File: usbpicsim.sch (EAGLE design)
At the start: 11 parts, among them U1 PIC16F1455-I/ST

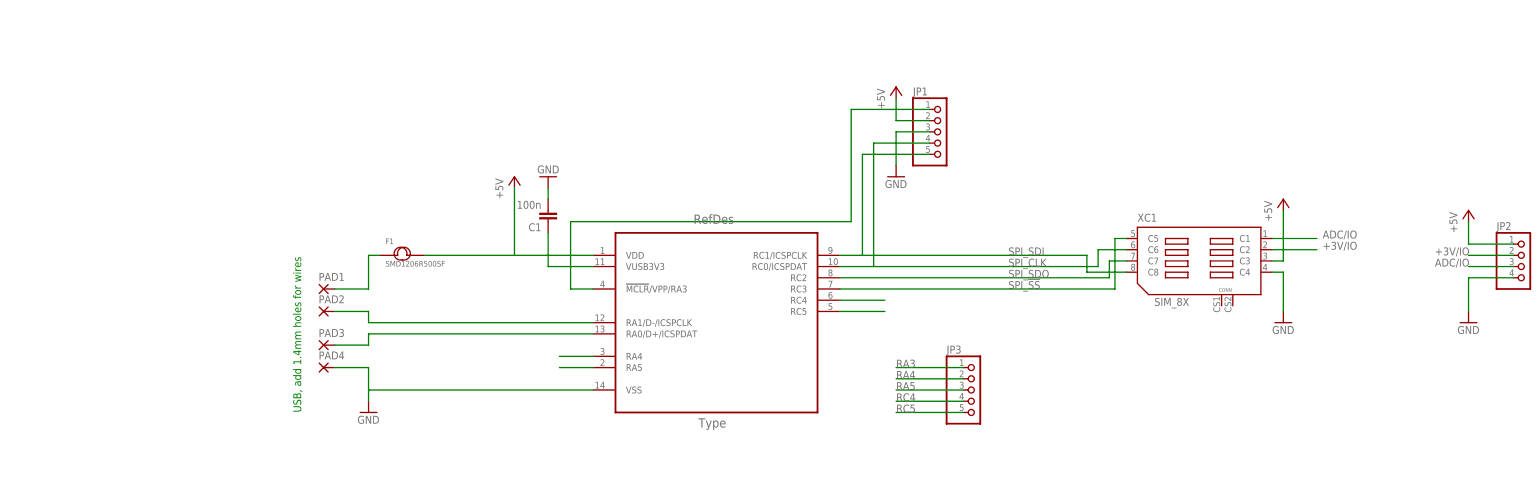
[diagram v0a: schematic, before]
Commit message: Use PIC LF (low voltage), add LDO
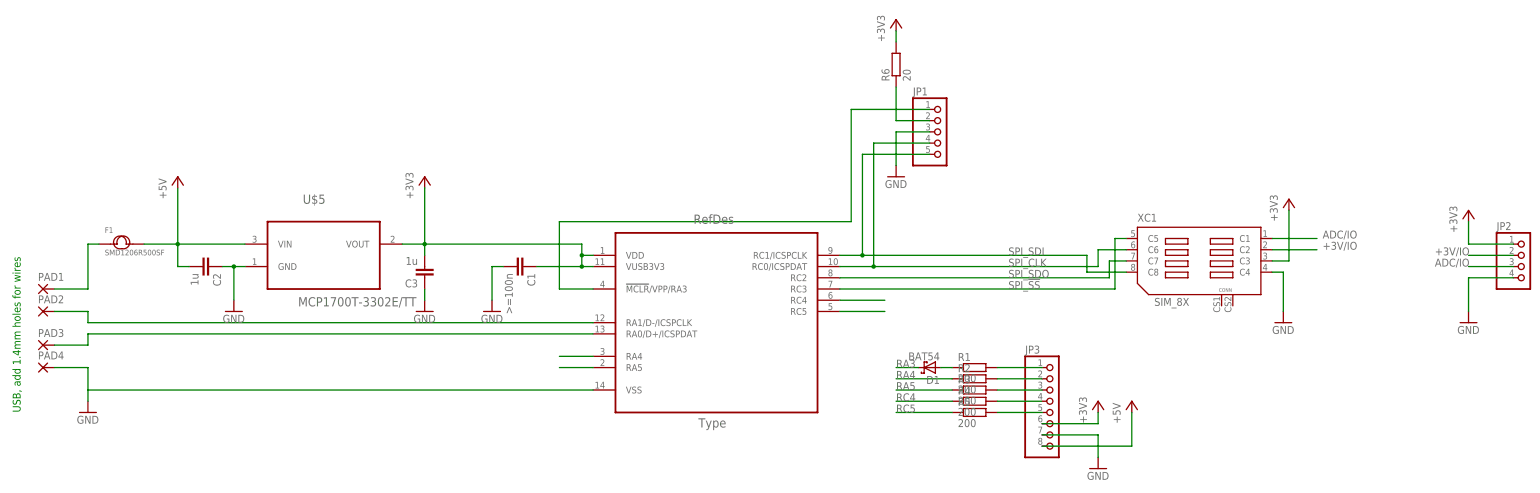
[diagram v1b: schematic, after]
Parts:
- added C2, C3: 1u, rcl:C-EUC0603
- added D1: BAT54, diode:BAT54
- added R1, R2, R3, R4, R5: 200, tagps:R-EU_R0603
- added R6: 20, tagps:R-EU_R0603
- added U$5: MCP1700T-3302E/TT, usbpiclib:MCP1700T-3302E/TT
- C1: value 100n -> >=100n
- JP3: device pinhead:PINHD-1X5 -> pinhead:PINHD-1X8
- U1: value PIC16F1455-I/ST -> PIC16LF1455-I/ST; device usbpiclib:PIC16F1455-I/ST -> usbpiclib:PIC16LF1455-I/ST
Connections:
- new net +3V3: C1.1, C3.2, JP2.1, JP3.6, R6.2, U$5.VOUT, U1.VDD, U1.VUSB3V3, XC1.C3
- new net N$10: D1.A, R1.1
- new net N$4: JP3.5, R5.2
- new net N$6: JP3.1, R1.2
- new net N$7: JP3.2, R2.2
- new net N$8: JP3.4, R4.2
- new net N$9: JP1.2, R6.1
- net +3V/IO: now also JP2.2
- net +5V: now also C2.2, JP3.8, U$5.VIN; no longer JP1.2, JP2.1, U1.VDD, XC1.C3
- net ADC/IO: now also JP2.3
- net GND: now also C2.1, C3.1, JP3.7, U$5.GND
- net N$1: now also JP3.3, R3.2; no longer C1.1, U1.VUSB3V3
- net RA3: now also D1.C; no longer JP3.1
- net RA4: now also R2.1; no longer JP3.2
- net RA5: now also R3.1; no longer JP3.3
- net RC4: now also R4.1; no longer JP3.4
- net RC5: now also R5.1; no longer JP3.5
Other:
- moved on the sheet: C1, F1, PAD1, PAD2, PAD3, PAD4

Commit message: Polish scheme, board
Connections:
- net N$10 renamed RA3@1
- net N$6 renamed RA3@2
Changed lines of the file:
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@@
 <setting verticaltext="up"/>
 </settings>
-<grid distance="0.1" unitdist="inch" unit="inch" style="lines" multiple="1" display="yes" altdistance="0.01" altunitdist="inch" altunit="inch"/>
+<grid distance="0.1" unitdist="inch" unit="inch" style="lines" multiple="1" display="no" altdistance="0.01" altunitdist="inch" altunit="inch"/>
 <layers>
 <layer number="1" name="Top" color="4" fill="1" visible="no" active="no"/>
@@
 </segment>
 </net>
-<net name="N$6" class="0">
+<net name="RA3@2" class="0">
 <segment>
 <pinref part="JP3" gate="A" pin="1"/>
@@
 </segment>
 </net>
-<net name="N$10" class="0">
+<net name="RA3@1" class="0">
 <segment>
 <pinref part="R1" gate="G$1" pin="1"/>

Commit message: Final usbpicsim board tuning
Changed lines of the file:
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@@
 <wire x1="-119.38" y1="40.64" x2="-111.76" y2="40.64" width="0.1524" layer="91"/>
 <wire x1="-111.76" y1="40.64" x2="-111.76" y2="35.56" width="0.1524" layer="91"/>
+<junction x="-111.76" y="35.56"/>
 </segment>
 <segment>

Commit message: Add TODO comment
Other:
- note added: "Pridat diodu jako ochranu proti prepolovani"
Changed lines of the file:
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@@
 <plain>
 <text x="-127" y="30.48" size="1.778" layer="91" rot="R90">USB, add 1.4mm holes for wires</text>
+<text x="-121.92" y="91.44" size="1.778" layer="91">Pridat diodu jako ochranu proti prepolovani</text>
 </plain>
 <instances>
